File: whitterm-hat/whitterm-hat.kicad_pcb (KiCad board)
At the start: 4 copper layers, 173.5 x 85 mm, 185 parts, among them IC1 SAMD21G18A, J1 USB_C_Receptacle, J2 Touch I2C, J3 40HAT, J4 DB9_Male, J5 Conn_02x05_Odd_Even, J6 Conn_01x04_Female, J7 Conn_01x04_Female, J8 Conn_01x10_Female, J9 CONN_01X02, Q1 IRLML6402PBF, Q2 IRLML6402PBF, Q3 BC850, Q4 BC850, Q5 BC850, Q6 BC850, Q7 IRLML6402PBF, Q8 IRLML6402PBF, Q9 IRLML6402PBF, SW1 SW_DIP_x06, U1 TUSB320, U10 ADA4807-2ARM, U11 ADA4807-2ARM, U2 CAT24C32, U3 74LVC1G17, U4 74LVC1G17, U5 MAX3221, U6 74LVC2G02, U9 MCP1703A-3302_SOT23, Y1 32.768

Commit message: pcb sent for production
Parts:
- removed the D13 at (174.7, -41.2)
- removed H1, H2, H3, H4: 3mm_Mounting_Hole, project_footprints:NPTH_3mm_ID
- removed the R30 at (167.8, -34.2)
- removed TP28, TP8, TP9: TestPoint, KiCad/TestPoint.pretty:TestPoint_Pad_D2.0mm
- removed U9: MCP1703A-3302_SOT23, KiCad/Package_TO_SOT_SMD.pretty:SOT-23
- added C22: 470pF, KiCad/Capacitor_SMD.pretty:C_0603_1608Metric, B.Cu at (125.0, 69.3)
- added C23: 10pF, KiCad/Capacitor_SMD.pretty:C_0603_1608Metric, B.Cu at (125.0, 72.3)
- added D10: SMAJ30A-TR, liubenyuan/kicad-xeit/xeit.pretty:D_DO-214AA, B.Cu at (209.8, 71.7)
- added D22: KP-2012MGC, KiCad/LED_SMD.pretty:LED_0603_1608Metric, F.Cu at (172.2, 46.6)
- added D23: KP-2012MGC, KiCad/LED_SMD.pretty:LED_0603_1608Metric, F.Cu at (165.2, 46.6)
- added D9: SMAJ30A-TR, liubenyuan/kicad-xeit/xeit.pretty:D_DO-214AA, B.Cu at (198.3, 71.7)
- added G***: LOGO, tunaf1sh/JBR-logos.pretty:jbr_logo_24, F.Cu at (200.5, 116.5)
- added G***: LOGO, tunaf1sh/JBR-logos.pretty:jbr_logo_48, B.Cu at (190.3, 113.9)
- added Q10: BC850, KiCad/Package_TO_SOT_SMD.pretty:SOT-23, B.Cu at (194.3, 71.5)
- added Q11: BC850, KiCad/Package_TO_SOT_SMD.pretty:SOT-23, B.Cu at (204.1, 71.7)
- added R58: 220R, KiCad/Resistor_SMD.pretty:R_0603_1608Metric, F.Cu at (163.6, 46.6)
- added R59: 470R, KiCad/Resistor_SMD.pretty:R_0603_1608Metric, B.Cu at (200.8, 71.7)
- added R60: 470R, KiCad/Resistor_SMD.pretty:R_0603_1608Metric, B.Cu at (212.3, 71.7)
- added R61: 1k, KiCad/Resistor_SMD.pretty:R_0603_1608Metric, B.Cu at (207.1, 71.7)
- added R62: 1k, KiCad/Resistor_SMD.pretty:R_0603_1608Metric, B.Cu at (191.3, 71.5)
- added R63: 470R, KiCad/Resistor_SMD.pretty:R_0603_1608Metric, B.Cu at (206.1, 68.7)
- added R64: 470R, KiCad/Resistor_SMD.pretty:R_0603_1608Metric, B.Cu at (198.3, 66.7)
- added R65: 9k1, KiCad/Resistor_SMD.pretty:R_0603_1608Metric, B.Cu at (128.3, 68.3)
- added R66: 110R, KiCad/Resistor_SMD.pretty:R_0603_1608Metric, F.Cu at (135.8, 51.7)
- added REF**: MountingHole_3.2mm_M3_ISO7380_Pad, KiCad/MountingHole.pretty:MountingHole_3.2mm_M3_ISO7380_Pad, F.Cu at (220.6, 116.6)
- added REF**: MountingHole_3.2mm_M3_ISO7380_Pad, KiCad/MountingHole.pretty:MountingHole_3.2mm_M3_ISO7380_Pad, F.Cu at (220.6, 46.0)
- added REF**: MountingHole_3.2mm_M3_ISO7380_Pad, KiCad/MountingHole.pretty:MountingHole_3.2mm_M3_ISO7380_Pad, F.Cu at (61.6, 46.0)
- added REF**: MountingHole_3.2mm_M3_ISO7380_Pad, KiCad/MountingHole.pretty:MountingHole_3.2mm_M3_ISO7380_Pad, F.Cu at (61.6, 116.6)
- added SW2: SW_Push, mcous/kicad-lib/footprints/switch.pretty:SPST-4-PIN_6mm_sm, F.Cu at (132.0, 47.6)
- added TP35: TestPoint, KiCad/TestPoint.pretty:TestPoint_Pad_D1.5mm, F.Cu at (192.0, 68.8)
- added TP36: TestPoint, KiCad/TestPoint.pretty:TestPoint_Pad_D1.5mm, F.Cu at (213.3, 68.7)
- added TP37: TestPoint, KiCad/TestPoint.pretty:TestPoint_Pad_D1.5mm, F.Cu at (188.8, 68.8)
- added U7: MCP1703A-3302_SOT23, KiCad/Package_TO_SOT_SMD.pretty:SOT-23, B.Cu at (177.1, 92.0)
- added svg2mod: G***, tunaf1sh/JBR-logos.pretty:whitterm220-fullname, F.Cu at (97.1, 46.0)
- added svg2mod: G***, tunaf1sh/JBR-logos.pretty:whitterm220-wt220, F.Cu at (143.0, 116.5)
- C1, C16, C17, C18, C19, C2, C20, C21, C3, C4, C6, D12, D14, D15, D16, D17, D18, D19, D20, D21, J2, J6, JP10, L2, Q1, Q3, Q4, Q5, Q6, R15, R16, R17, R20, R34, R35, R36, R37, R38, R39, R40, R41, R42, R43, R44, R45, R46, R49, R50, R51, R52, R53, U10, U11, U5: moved to B.Cu
- D24: value SMAJ30A-TR -> SMAJ12A-TR; moved to B.Cu
- D8: footprint KiCad/Package_TO_SOT_THT.pretty:TO-92_Inline -> KiCad/Package_SO.pretty:SOIC-8_3.9x4.9mm_P1.27mm
- J3: footprint KiCad/Connector_PinHeader_2.54mm.pretty:PinHeader_2x20_P2.54mm_Vertical -> greatscottgadgets/gsg-kicad-lib/gsg-modules.pretty:HEADER-2x20-REVERSE
- R13: value 3k9 -> 50k; moved to B.Cu
- R14: value 9k1 -> 100k; moved to B.Cu
- TP1, TP10, TP11, TP12, TP13, TP14, TP15, TP16, TP17, TP18, TP19, TP2, TP20, TP21, TP22, TP23, TP24, TP25, TP26, TP27, TP29, TP3, TP30, TP31, TP32, TP33, TP34, TP4, TP5, TP6, TP7: footprint KiCad/TestPoint.pretty:TestPoint_Pad_D2.0mm -> KiCad/TestPoint.pretty:TestPoint_Pad_D1.5mm
- moved R20 163.8 mm to (180.3, 94.8), turned to 180 degrees
- moved TP5 161.8 mm to (201.6, 102.6)
- moved JP6 160.1 mm to (208.6, 93.3), turned to 90 degrees
- moved TP4 159.9 mm to (204.6, 102.6)
- moved U4 158.4 mm to (202.6, 88.3), turned to 180 degrees
- moved JP5 157.5 mm to (206.1, 93.3), turned to 90 degrees
- moved R3 156.5 mm to (207.4, 101.8), turned to 90 degrees
- moved R1 155.1 mm to (210.6, 100.0)
- moved TP7 155.1 mm to (211.2, 88.8)
- moved R4 154.9 mm to (210.6, 98.2), turned to 180 degrees
- moved TP3 154.4 mm to (198.2, 102.6)
- moved U5 154.3 mm to (183.0, 72.1), turned to 180 degrees
- moved D1 154.0 mm to (193.4, 102.6)
- moved R5 153.2 mm to (210.6, 96.5)
- moved J4 152.4 mm to (189.1, 58.8)
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- renumbered D23 to D13, R31 to R30, R32 to R31, R58 to R32
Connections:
- D16 pad 2: Net-(C19-Pad1) -> GND
- D16 pad 3: VCC -> Net-(C19-Pad1)
- D17 pad 1: Net-(C18-Pad1) -> VCC
- D17 pad 3: GND -> Net-(C18-Pad1)
- D8 pad 2: Net-(C7-Pad1) -> (no net)
- D8 pad 3: GND -> (no net)
- IC1 pad 13: /microcontroller/D4 -> /U_CTS
- IC1 pad 22: (no net) -> Net-(IC1-Pad22)
- IC1 pad 25: (no net) -> /microcontroller/D11
- IC1 pad 27: /microcontroller/D10 -> /U_RTS
- IC1 pad 28: (no net) -> /microcontroller/D12
- IC1 pad 37: (no net) -> Net-(IC1-Pad37)
- IC1 pad 38: (no net) -> Net-(IC1-Pad38)
- IC1 pad 41: (no net) -> /microcontroller/USB_H_EN
- IC1 pad 47: (no net) -> Net-(IC1-Pad47)
- J1 pad A10: (no net) -> Net-(J1-PadA10)
- J1 pad A11: (no net) -> Net-(J1-PadA11)
- J1 pad A2: (no net) -> Net-(J1-PadA2)
- J1 pad A3: (no net) -> Net-(J1-PadA3)
- J1 pad A8: (no net) -> Net-(J1-PadA8)
- J1 pad B10: (no net) -> Net-(J1-PadB10)
- J1 pad B11: (no net) -> Net-(J1-PadB11)
- J1 pad B2: (no net) -> Net-(J1-PadB2)
- J1 pad B3: (no net) -> Net-(J1-PadB3)
- J1 pad B8: (no net) -> Net-(J1-PadB8)
- J2 pad 4: (no net) -> Net-(J2-Pad4)
- J3 pad 12: (no net) -> Net-(J3-Pad12)
- J3 pad 15: (no net) -> Net-(J3-Pad15)
- J3 pad 16: (no net) -> Net-(J3-Pad16)
- J3 pad 17: (no net) -> Net-(J3-Pad17)
- J3 pad 18: (no net) -> Net-(J3-Pad18)
- J3 pad 19: (no net) -> /PI_MOSI
- J3 pad 21: (no net) -> /PI_MISO
- J3 pad 22: (no net) -> Net-(J3-Pad22)
- J3 pad 23: (no net) -> /PI_SCLK
- J3 pad 24: (no net) -> /PI_CE0
- J3 pad 26: (no net) -> /PI_CE1
- J3 pad 29: (no net) -> Net-(J3-Pad29)
- J3 pad 31: (no net) -> Net-(J3-Pad31)
- J3 pad 32: (no net) -> Net-(J3-Pad32)
- J3 pad 33: (no net) -> Net-(J3-Pad33)
- J3 pad 35: (no net) -> Net-(J3-Pad35)
- J3 pad 36: (no net) -> Net-(J3-Pad36)
- J3 pad 37: (no net) -> Net-(J3-Pad37)
- J3 pad 38: (no net) -> Net-(J3-Pad38)
- J3 pad 40: (no net) -> Net-(J3-Pad40)
- J3 pad 7: (no net) -> Net-(J3-Pad7)
- J4 pad 1: (no net) -> Net-(J4-Pad1)
- J4 pad 4: (no net) -> Net-(J4-Pad4)
- J4 pad 6: (no net) -> Net-(J4-Pad6)
- J4 pad 7: (no net) -> /RS232-UART/RS232_RTS
- J4 pad 8: (no net) -> /RS232-UART/RS232_CTS
- J4 pad 9: (no net) -> Net-(J4-Pad9)
- J5 pad 6: (no net) -> Net-(J5-Pad6)
- J5 pad 7: (no net) -> Net-(J5-Pad7)
- J5 pad 8: (no net) -> Net-(J5-Pad8)
- J5 pad 9: (no net) -> Net-(J5-Pad9)
- R20 pad 1: /~RPI_EN_ACT -> Net-(D12-Pad2)
- R20 pad 2: VCC -> GND
- U11 pad 3: /microcontroller/A0_DAC -> Net-(C22-Pad1)
- U11 pad 7: (no net) -> Net-(U11-Pad7)
- U5 pad 10: (no net) -> Net-(U5-Pad10)
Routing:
- net VCC: track 0.00 -> 496.6 mm, vias 0 -> 37
- net /microcontroller/A2: track 0.00 -> 187.6 mm, vias 0 -> 7
- net /microcontroller/D13: track 0.00 -> 184.4 mm, vias 0 -> 4
- net /U_CTS: track 0.00 -> 178.4 mm, vias 0 -> 3
- net /PI_3V3: track 0.00 -> 176.3 mm, vias 0 -> 4
- net /USBC_SCL: track 0.00 -> 172.0 mm, vias 0 -> 6
- net /PI_RXD: track 0.00 -> 171.2 mm, vias 0 -> 2
- net /PI_TXD: track 0.00 -> 170.5 mm, vias 0 -> 4
- net /USBC_SDA: track 0.00 -> 168.9 mm, vias 0 -> 6
- net /U_RTS: track 0.00 -> 162.5 mm, vias 0 -> 3
- net /SAMD_TXD: track 0.00 -> 162.4 mm, vias 0 -> 4
- net Net-(R23-Pad2): track 0.00 -> 158.5 mm, vias 0 -> 4
- net /SAMD_RXD: track 0.00 -> 157.0 mm, vias 0 -> 4
- net /microcontroller/D11: track 0.00 -> 148.4 mm, vias 0 -> 4
- net Net-(R22-Pad1): track 0.00 -> 146.2 mm, vias 0 -> 4
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- added copper zone on B.Cu, net GND
- added copper zone on F.Cu, net GND
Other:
- outline, holes or cut-outs redrawn
- copper layers 4 -> 2
- net class Default: via_dia 0.4 -> 0.5
- rule via_min_size: 0.4 -> 0.5
- board text added: "* 5 V In * SAMD UART"
- board text added: "* ON ONLY IN PAIRS AND ONE PAIR ONLY!"
- board text added: "3V3"
- board text added: "5V"
- board text added: "AIN1"
- board text added: "AIN2"
- board text added: "AOUT"
- board text added: "Analogue: 0 - 10 V Digital: 0 - 24 V O: STG / I: NPN"
- board text added: "Blink"
- board text added: "Boot"
- board text added: "Buffered IO"
- board text added: "DIN1"
- board text added: "DIN2"
- board text added: "DOUT1"
- board text added: "DOUT2"
- board text added: "GND"
- board text added: "OUT1: 1.5 / 3 A"
- board text added: "OUT2: 0.5 / 3 A"
- board text added: "Pi GPIO"
- board text added: "Pi USB"
- board text added: "RPi"
- board text added: "RPi UART"
- board text added: "RS232"
- board text added: "RX"
- board text added: "SAMD UART"
- board text added: "SAMD UART -> RPi UART"
- board text added: "Status"
- board text added: "TTL RS232 -> RPi UART"
- board text added: "TTL RS232 -> SAMD UART"
- board text added: "TX"
- board text added: "USB-C"
- board text added: "WT-220 Hat - April 2019 - 1.0"
- board text added: "Whitterm 220 clever serial terminal"

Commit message: button button logic
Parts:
- D14, D15: value BZX84Cxx -> BZX84C10LT1G
- D7: value RXD -> TXD
- R66: value 110R -> 10k
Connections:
- net /PI_CE0 renamed Net-(J3-Pad24)
- net /PI_CE1 renamed Net-(J3-Pad26)
- net /PI_MISO renamed Net-(J3-Pad21)
- net /PI_MOSI renamed Net-(J3-Pad19)
- net /PI_SCLK renamed Net-(J3-Pad23)
- D16 pad 2: GND -> Net-(C19-Pad1)
- D16 pad 3: Net-(C19-Pad1) -> GND
- D17 pad 2: GND -> Net-(C18-Pad1)
- D17 pad 3: Net-(C18-Pad1) -> GND

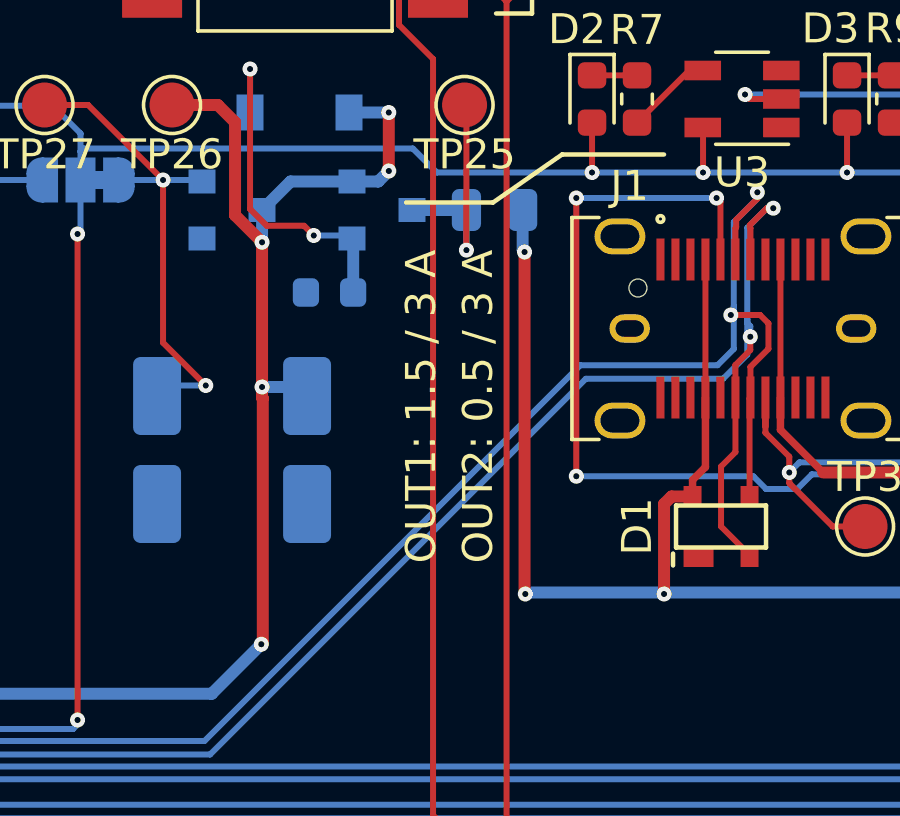
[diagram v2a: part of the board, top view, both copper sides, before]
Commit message: mods during bring up, see notes
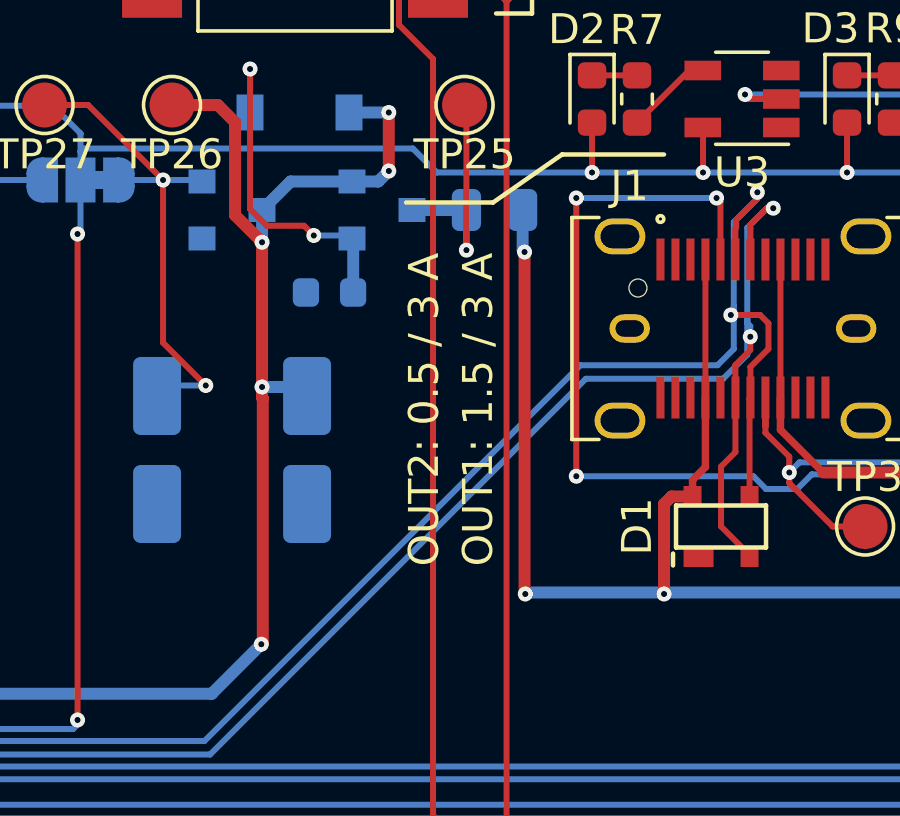
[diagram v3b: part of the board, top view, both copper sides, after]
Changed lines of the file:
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@@
   (gr_line (start 185.8 91.8) (end 188.1 90.2) (layer F.SilkS) (width 0.15))
   (gr_line (start 182.9 91.8) (end 185.8 91.8) (layer F.SilkS) (width 0.15))
-  (gr_text "OUT1: 1.5 / 3 A" (at 183.4 98.6 90) (layer F.SilkS)
+  (gr_text "OUT1: 1.5 / 3 A" (at 185.3 98.7 90) (layer F.SilkS)
     (effects (font (size 1 1) (thickness 0.15)))
   )
-  (gr_text "OUT2: 0.5 / 3 A" (at 185.3 98.6 90) (layer F.SilkS)
+  (gr_text "OUT2: 0.5 / 3 A" (at 183.5 98.7 90) (layer F.SilkS)
     (effects (font (size 1 1) (thickness 0.15)))
   )

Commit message: firmware functionally complete for basic button usage
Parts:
- added J10: Conn_01x04_Female, KiCad/Connector_PinHeader_2.54mm.pretty:PinHeader_1x04_P2.54mm_Vertical, F.Cu at (212.3, 55.5)
- added Q12: BC850, KiCad/Package_TO_SOT_SMD.pretty:SOT-23, F.Cu at (135.0, 93.2)
- added R31: 10k, KiCad/Resistor_SMD.pretty:R_0603_1608Metric, F.Cu at (196.1, 85.5)
- added R67: 10k, KiCad/Resistor_SMD.pretty:R_0603_1608Metric, F.Cu at (203.2, 91.7)
- D8: value LM285Z-1.2 -> LM285D-2.5G
- R10, R12, R47, R48, R6, R8: value 3.9K -> 4.7K
- R13: value 50k -> 100k
- R18, R19, R22, R23, R26, R27, R28, R7, R9: value 110R -> 150R
- R65: value 9k1 -> 1k
- U2: value CAT24C32 -> CAT24C32WI-GT3
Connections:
- C21 pad 2: VCC -> +5V
- IC1 pad 14: /~PI_EN -> /PI_EN
- J8 pad 5: /buffers/DIN_O1 -> /buffers/DIN_I1
- J8 pad 6: /buffers/DIN_O2 -> /buffers/DIN_I2
- Q2 pad 1: Net-(Q2-Pad1) -> Net-(Q12-Pad3)
- R30 pad 2: Net-(Q2-Pad1) -> Net-(Q12-Pad3)
- R43 pad 1: /buffers/DIN_O1 -> /microcontroller/D8
- R46 pad 2: /microcontroller/D8 -> /buffers/DIN_I1
- R50 pad 1: /buffers/DIN_O2 -> /microcontroller/D9
- R53 pad 2: /microcontroller/D9 -> /buffers/DIN_I2
- U11 pad 8: VCC -> +5V
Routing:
- net /buffers/DIN_I1: track 0.00 -> 46.3 mm, vias 0 -> 2
- net /buffers/DIN_O1: track 31.5 -> 0.00 mm, vias 1 -> 0
- net /buffers/DIN_I2: track 0.00 -> 28.2 mm, vias 0 -> 2
- net /buffers/DIN_O2: track 15.7 -> 0.00 mm
- net /microcontroller/D8: track 81.2 -> 89.6 mm
- net /microcontroller/D9: track 88.5 -> 96.6 mm
- net Net-(Q2-Pad1): track 6.17 -> 0.00 mm
- net /~PI_EN: track 37.1 -> 31.1 mm
- net GND: track 43.3 -> 47.9 mm
- net VCC: track 496.6 -> 492.3 mm, vias 37 -> 36
- net Net-(C19-Pad1): track 10.3 -> 12.6 mm
- net Net-(C18-Pad1): track 12.6 -> 13.3 mm

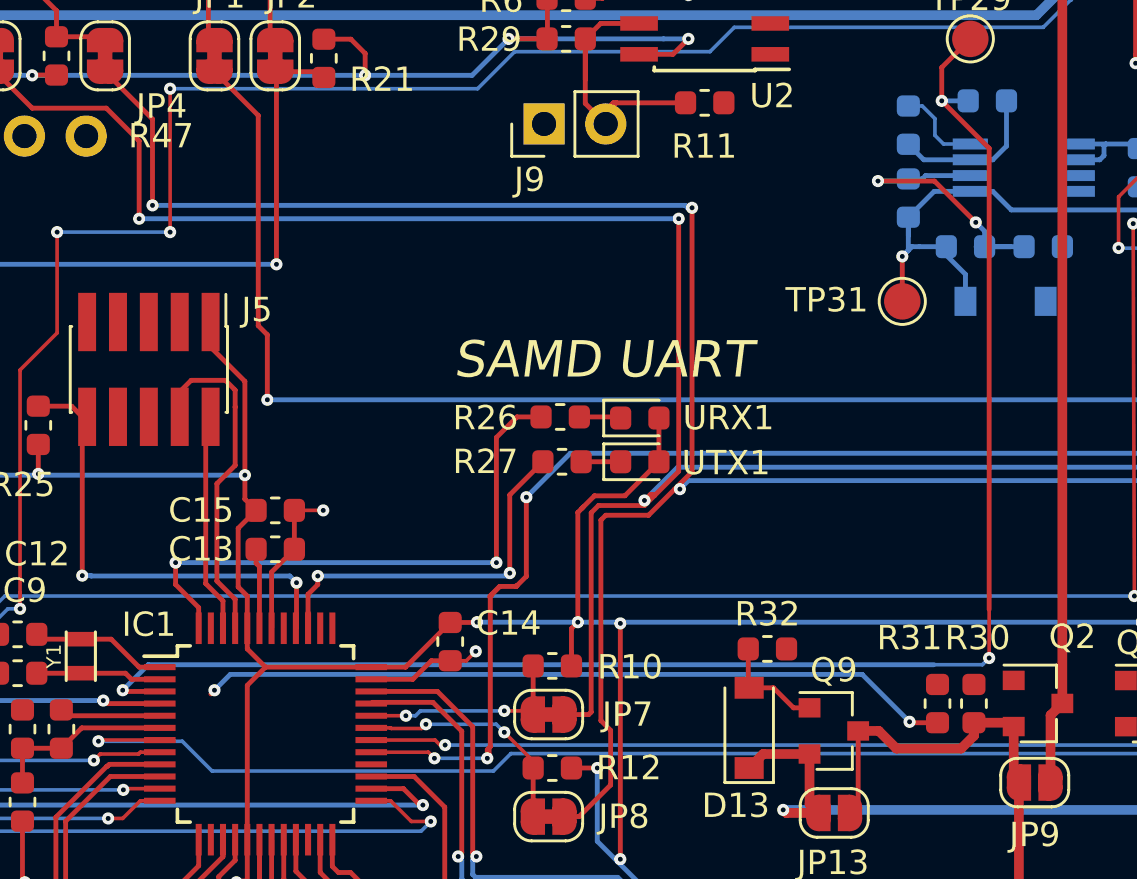
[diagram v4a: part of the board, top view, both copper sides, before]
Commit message: remove abort shutdown so that hard shutdown available
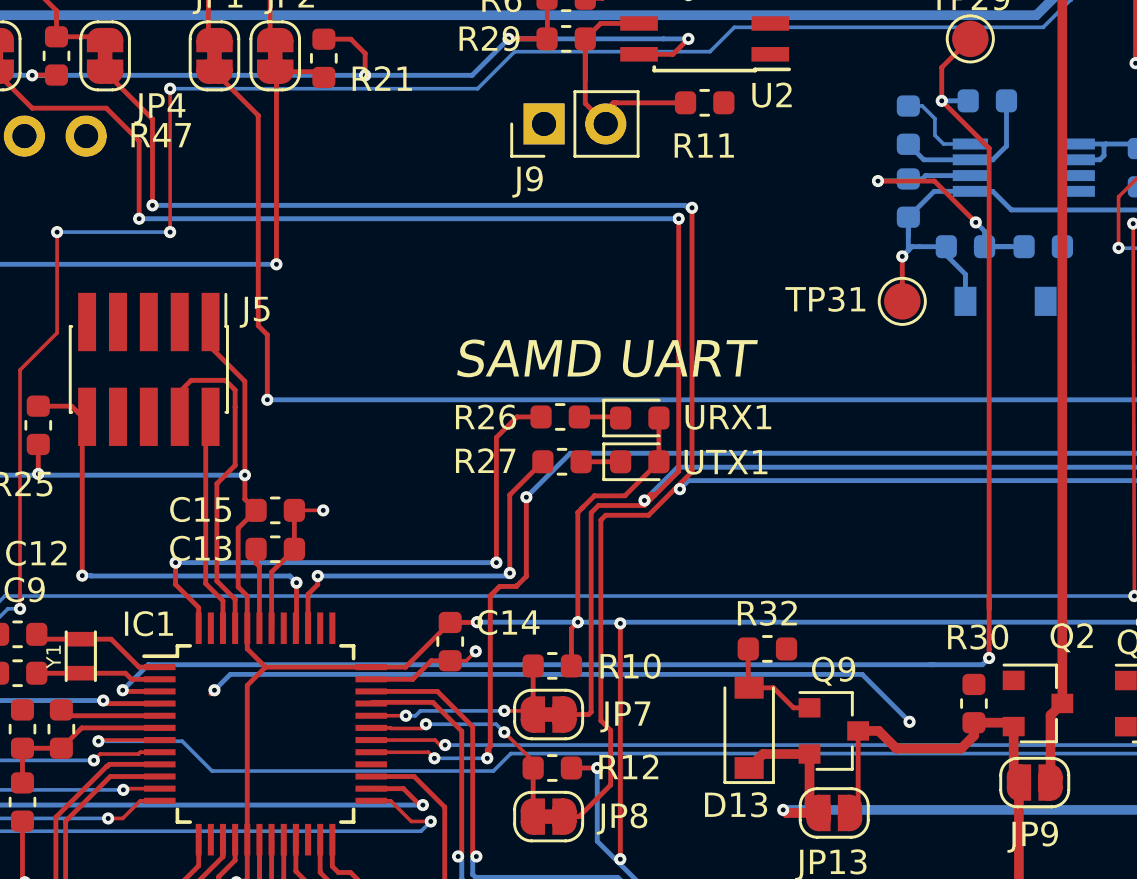
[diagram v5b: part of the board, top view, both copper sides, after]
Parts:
- removed the R31 at (126.2, 93.2)
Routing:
- net /microcontroller/A0_DAC: track 65.6 -> 70.2 mm
- net /~PI_EN: track 31.1 -> 29.9 mm
